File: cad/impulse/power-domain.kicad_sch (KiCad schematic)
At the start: 24 parts, among them Q101 AO3415, U2 MT2492, U3 MT2492

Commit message: Finished with schematic, starting to route traces.
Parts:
- C11, C12, C14, C18: footprint (none) -> Capacitor_SMD:C_0402_1005Metric
- C13, C15, C16, C17, C19, C20: footprint (none) -> Capacitor_SMD:C_1206_3216Metric
- D1: footprint (none) -> Diode_SMD:D_SOD-123F
- D2: footprint (none) -> Diode_SMD:D_SOD-323
- FB1: footprint (none) -> Resistor_SMD:R_0805_2012Metric
- JP101: footprint (none) -> Jumper:SolderJumper-2_P1.3mm_Bridged2Bar_Pad1.0x1.5mm
- L1: footprint (none) -> Inductor_SMD:L_1210_3225Metric
- L2: footprint (none) -> Inductor_SMD:L_Sunlord_MWSA0402S
- Q101: footprint (none) -> Package_TO_SOT_SMD:SOT-23
- R101, R6, R7, R8, R9: footprint (none) -> Resistor_SMD:R_0402_1005Metric
- U2, U3: footprint (none) -> Package_TO_SOT_SMD:SOT-23-6
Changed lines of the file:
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@@
       (effects (font (size 1.27 1.27)) (justify left))
     )
-    (property "Footprint" "" (at 127 36.83 0)
+    (property "Footprint" "Resistor_SMD:R_0402_1005Metric" (at 127 36.83 0)
       (effects (font (size 1.27 1.27)) hide)
     )
@@
       (effects (font (size 1.27 1.27)))
     )
-    (property "Footprint" "" (at 124.46 29.21 0)
+    (property "Footprint" "Inductor_SMD:L_1210_3225Metric" (at 124.46 29.21 0)
       (effects (font (size 1.27 1.27)) hide)
     )
@@
       (effects (font (size 1.27 1.27)))
     )
-    (property "Footprint" "" (at 35.56 27.94 0)
+    (property "Footprint" "Package_TO_SOT_SMD:SOT-23" (at 35.56 27.94 0)
       (effects (font (size 1.27 1.27)) hide)
     )
@@
       (effects (font (size 1.27 1.27)))
     )
-    (property "Footprint" "" (at 96.52 31.75 0)
+    (property "Footprint" "Capacitor_SMD:C_1206_3216Metric" (at 96.52 31.75 0)
       (effects (font (size 1.27 1.27)) hide)
     )
@@
       (effects (font (size 1.27 1.27)))
     )
-    (property "Footprint" "" (at 247.65 31.75 0)
+    (property "Footprint" "Capacitor_SMD:C_1206_3216Metric" (at 247.65 31.75 0)
       (effects (font (size 1.27 1.27)) hide)
     )
@@
       (effects (font (size 1.27 1.27)) (justify left))
     )
-    (property "Footprint" "" (at 210.82 15.24 0)
+    (property "Footprint" "Package_TO_SOT_SMD:SOT-23-6" (at 210.82 15.24 0)
       (effects (font (size 1.27 1.27)) hide)
     )
@@
       (effects (font (size 1.27 1.27)) (justify left))
     )
-    (property "Footprint" "" (at 38.1 41.91 0)
+    (property "Footprint" "Resistor_SMD:R_0402_1005Metric" (at 38.1 41.91 0)
       (effects (font (size 1.27 1.27)) hide)
     )
@@
       (effects (font (size 1.27 1.27)))
     )
-    (property "Footprint" "" (at 195.58 31.75 0)
+    (property "Footprint" "Capacitor_SMD:C_1206_3216Metric" (at 195.58 31.75 0)
       (effects (font (size 1.27 1.27)) hide)
     )
@@
       (effects (font (size 1.27 1.27)))
     )
-    (property "Footprint" "" (at 137.16 31.75 0)
+    (property "Footprint" "Capacitor_SMD:C_0402_1005Metric" (at 137.16 31.75 0)
       (effects (font (size 1.27 1.27)) hide)
     )
@@
       (effects (font (size 1.27 1.27)) (justify left))
     )
-    (property "Footprint" "" (at 127 31.75 0)
+    (property "Footprint" "Resistor_SMD:R_0402_1005Metric" (at 127 31.75 0)
       (effects (font (size 1.27 1.27)) hide)
     )
@@
       (effects (font (size 1.27 1.27)) (justify left))
     )
-    (property "Footprint" "" (at 45.72 35.56 90)
+    (property "Footprint" "Diode_SMD:D_SOD-323" (at 45.72 35.56 90)
       (effects (font (size 1.27 1.27)) hide)
     )
@@
       (effects (font (size 1.27 1.27)))
     )
-    (property "Footprint" "" (at 223.52 29.21 0)
+    (property "Footprint" "Inductor_SMD:L_Sunlord_MWSA0402S" (at 223.52 29.21 0)
       (effects (font (size 1.27 1.27)) hide)
     )
@@
       (effects (font (size 1.27 1.27)))
     )
-    (property "Footprint" "" (at 148.59 31.75 0)
+    (property "Footprint" "Capacitor_SMD:C_1206_3216Metric" (at 148.59 31.75 0)
       (effects (font (size 1.27 1.27)) hide)
     )
@@
       (effects (font (size 1.27 1.27)))
     )
-    (property "Footprint" "" (at 152.4 31.75 0)
+    (property "Footprint" "Capacitor_SMD:C_1206_3216Metric" (at 152.4 31.75 0)
       (effects (font (size 1.27 1.27)) hide)
     )
@@
       (effects (font (size 1.27 1.27)))
     )
-    (property "Footprint" "" (at 116.84 24.13 0)
+    (property "Footprint" "Capacitor_SMD:C_0402_1005Metric" (at 116.84 24.13 0)
       (effects (font (size 1.27 1.27)) hide)
     )
@@
       (effects (font (size 1.27 1.27)) (justify left))
     )
-    (property "Footprint" "" (at 111.76 15.24 0)
+    (property "Footprint" "Package_TO_SOT_SMD:SOT-23-6" (at 111.76 15.24 0)
       (effects (font (size 1.27 1.27)) hide)
     )
@@
       (effects (font (size 1.27 1.27)))
     )
-    (property "Footprint" "" (at 259.08 29.21 0)
+    (property "Footprint" "Jumper:SolderJumper-2_P1.3mm_Bridged2Bar_Pad1.0x1.5mm" (at 259.08 29.21 0)
       (effects (font (size 1.27 1.27)) hide)
     )
@@
       (effects (font (size 1.27 1.27)))
     )
-    (property "Footprint" "" (at 215.9 24.13 0)
+    (property "Footprint" "Capacitor_SMD:C_0402_1005Metric" (at 215.9 24.13 0)
       (effects (font (size 1.27 1.27)) hide)
     )
@@
       (effects (font (size 1.27 1.27)))
     )
-    (property "Footprint" "" (at 251.46 31.75 0)
+    (property "Footprint" "Capacitor_SMD:C_1206_3216Metric" (at 251.46 31.75 0)
       (effects (font (size 1.27 1.27)) hide)
     )
@@
       (effects (font (size 1.27 1.27)) (justify left))
     )
-    (property "Footprint" "" (at 226.06 36.83 0)
+    (property "Footprint" "Resistor_SMD:R_0402_1005Metric" (at 226.06 36.83 0)
       (effects (font (size 1.27 1.27)) hide)
     )
@@
       (effects (font (size 1.27 1.27)) (justify left))
     )
-    (property "Footprint" "" (at 226.06 31.75 0)
+    (property "Footprint" "Resistor_SMD:R_0402_1005Metric" (at 226.06 31.75 0)
       (effects (font (size 1.27 1.27)) hide)
     )
@@
       (effects (font (size 1.27 1.27)))
     )
-    (property "Footprint" "" (at 236.22 31.75 0)
+    (property "Footprint" "Capacitor_SMD:C_0402_1005Metric" (at 236.22 31.75 0)
       (effects (font (size 1.27 1.27)) hide)
     )
@@
       (effects (font (size 1.27 1.27)) (justify right))
     )
-    (property "Footprint" "" (at 48.26 20.32 90)
+    (property "Footprint" "Diode_SMD:D_SOD-123F" (at 48.26 20.32 90)
       (effects (font (size 1.27 1.27)) hide)
     )
@@
       (effects (font (size 1.27 1.27)))
     )
-    (property "Footprint" "" (at 58.42 32.258 90)
-      (effects (font (size 1.27 1.27)) hide)
-    )
+    (property "Footprint" "Resistor_SMD:R_0805_2012Metric" (at 58.42 32.258 90)
+      (effects (font (size 1.27 1.27)) hide)
+    )

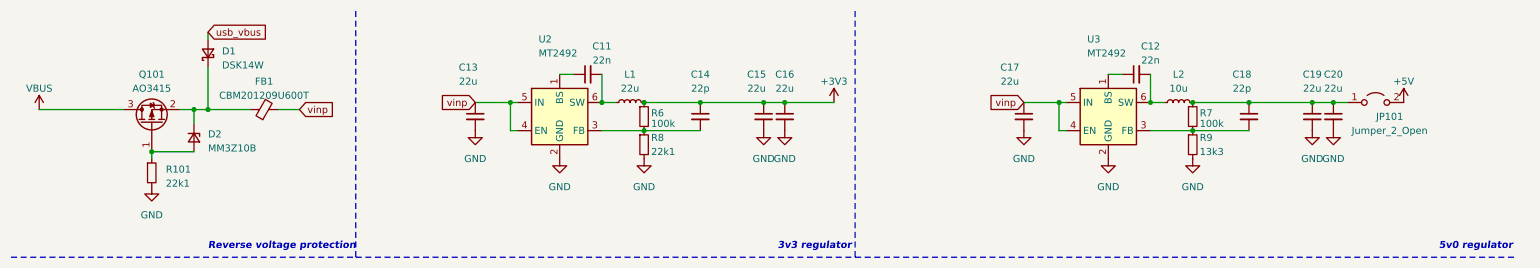
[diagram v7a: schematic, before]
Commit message: Modified oscillator circuit.
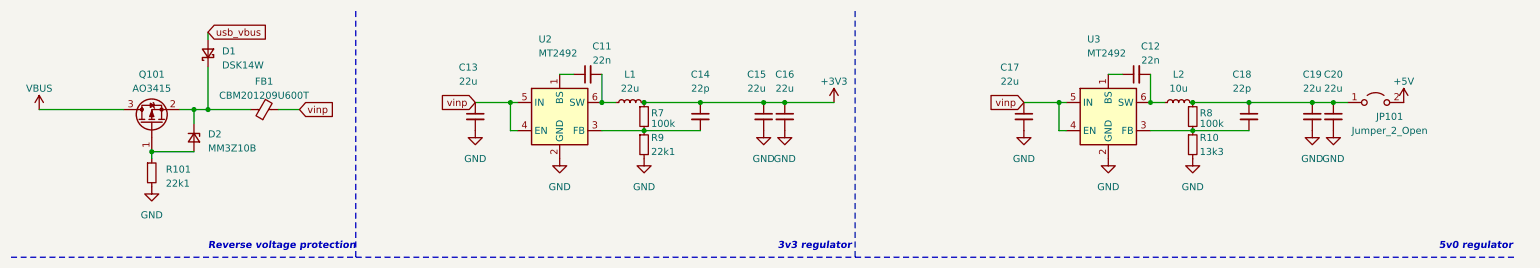
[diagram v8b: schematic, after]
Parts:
- renumbered R9 to R10, R6 to R7, R7 to R8, R8 to R9
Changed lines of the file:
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@@
   (symbol (lib_id "Device:R_Small") (at 127 36.83 0) (unit 1)
     (in_bom yes) (on_board yes) (dnp no)
-    (property "Reference" "R8" (at 128.27 35.56 0)
+    (property "Reference" "R9" (at 128.27 35.56 0)
       (effects (font (size 1.27 1.27)) (justify left))
     )
@@
       (project "impulse"
         (path "/eb4cfece-5fcb-437a-ac58-337ab6512039/8b8b63e5-7f69-4185-825a-2602e0d2cd2e"
-          (reference "R8") (unit 1)
+          (reference "R9") (unit 1)
         )
       )
@@
       (project "impulse"
         (path "/eb4cfece-5fcb-437a-ac58-337ab6512039/8b8b63e5-7f69-4185-825a-2602e0d2cd2e"
-          (reference "R10") (unit 1)
+          (reference "R11") (unit 1)
         )
       )
@@
   (symbol (lib_id "Device:R_Small") (at 127 31.75 0) (unit 1)
     (in_bom yes) (on_board yes) (dnp no)
-    (property "Reference" "R6" (at 128.27 31.115 0)
+    (property "Reference" "R7" (at 128.27 31.115 0)
       (effects (font (size 1.27 1.27)) (justify left))
     )
@@
       (project "impulse"
         (path "/eb4cfece-5fcb-437a-ac58-337ab6512039/8b8b63e5-7f69-4185-825a-2602e0d2cd2e"
-          (reference "R6") (unit 1)
+          (reference "R7") (unit 1)
         )
       )
@@
   (symbol (lib_id "Device:R_Small") (at 226.06 36.83 0) (unit 1)
     (in_bom yes) (on_board yes) (dnp no)
-    (property "Reference" "R9" (at 227.33 35.56 0)
+    (property "Reference" "R10" (at 227.33 35.56 0)
       (effects (font (size 1.27 1.27)) (justify left))
     )
@@
       (project "impulse"
         (path "/eb4cfece-5fcb-437a-ac58-337ab6512039/8b8b63e5-7f69-4185-825a-2602e0d2cd2e"
-          (reference "R9") (unit 1)
+          (reference "R10") (unit 1)
         )
       )
@@
   (symbol (lib_id "Device:R_Small") (at 226.06 31.75 0) (unit 1)
     (in_bom yes) (on_board yes) (dnp no)
-    (property "Reference" "R7" (at 227.33 31.115 0)
+    (property "Reference" "R8" (at 227.33 31.115 0)
       (effects (font (size 1.27 1.27)) (justify left))
     )
@@
       (project "impulse"
         (path "/eb4cfece-5fcb-437a-ac58-337ab6512039/8b8b63e5-7f69-4185-825a-2602e0d2cd2e"
-          (reference "R7") (unit 1)
-        )
-      )
+          (reference "R8") (unit 1)
+        )
+      )
